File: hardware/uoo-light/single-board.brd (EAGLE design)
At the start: 49.5 x 48.3 mm, 27 parts

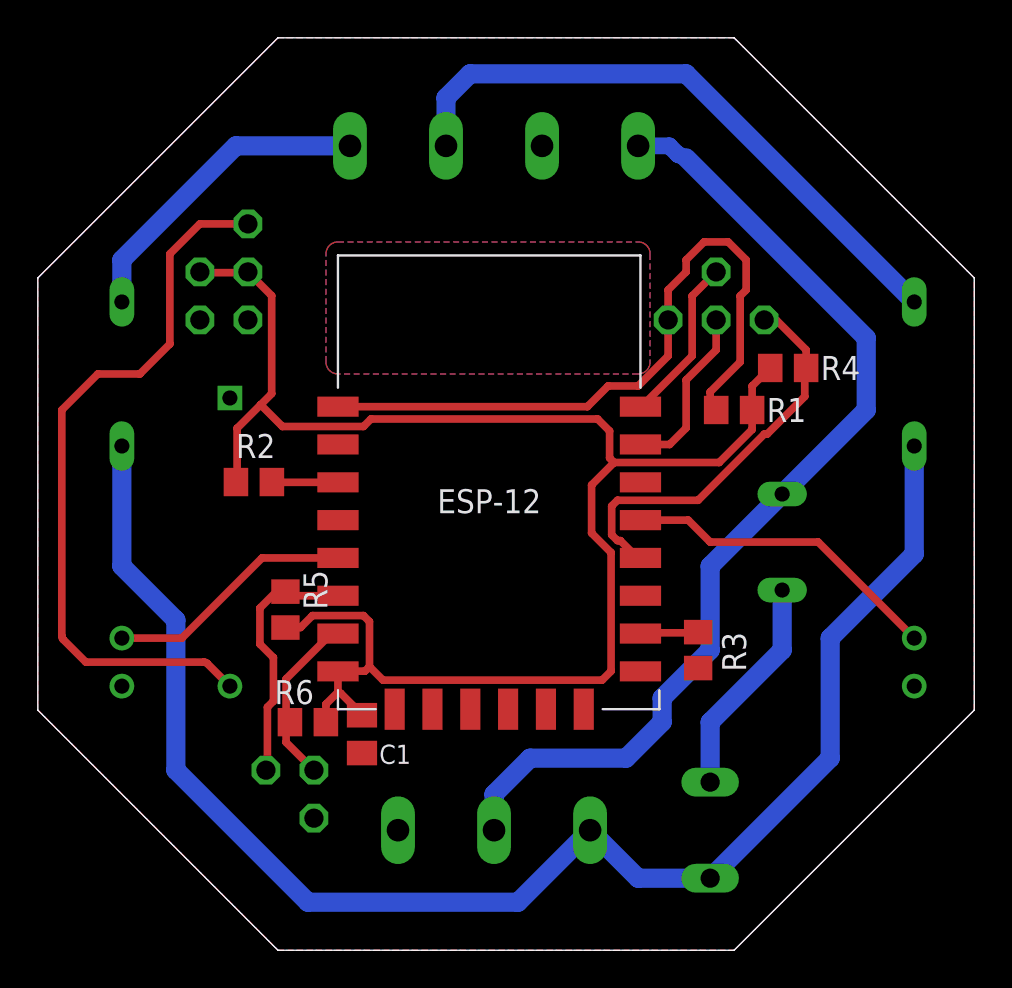
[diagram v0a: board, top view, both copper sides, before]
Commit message: second version of board. Mirrored elecromagnetic reeds, shorter pads in esp-12, better paths.added mount hole, bigger holes in my elements in library.
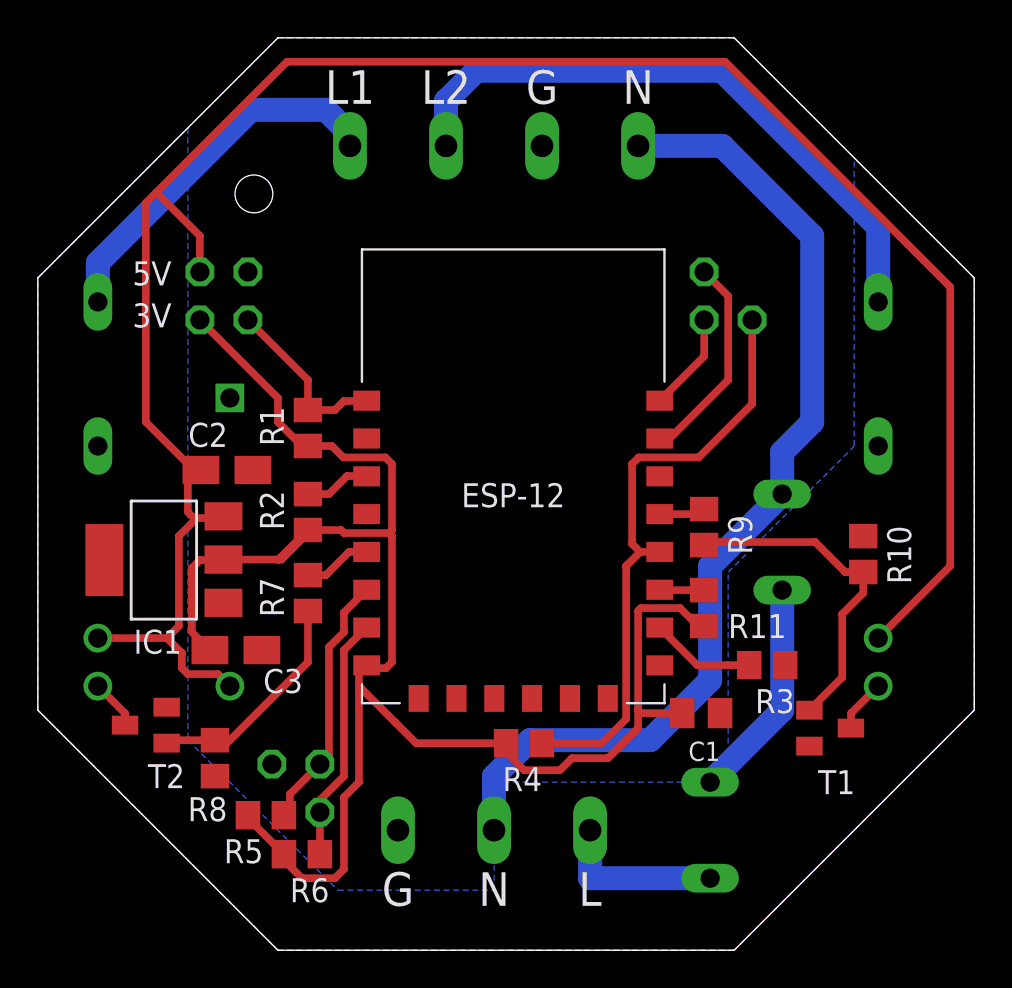
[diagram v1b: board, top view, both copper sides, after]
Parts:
- removed 3V1: 3V, pinhead:1X01
- removed GND8: GND, pinhead:1X01
- added C2, C3: (no value), rcl:A/3216-18R
- added IC1: REG1117, burr-brown:SOT223
- added R10, R11, R7, R8, R9: (no value), rcl:R0805
- added T1, T2: BC847, transistor:SOT23
- C1: value (none) -> 100nF
- G: value (none) -> G
- IN: value (none) -> AC IN
- L: value (none) -> LOUT
- OUT: value (none) -> OUT
- S1: value (none) -> S1
- S2: value (none) -> S2
- moved R4 24.3 mm to (28.9, 14.1)
- moved R1 22.6 mm to (17.5, 30.8), turned to 90 degrees
- moved RST 22.2 mm to (14.3, 36.5)
- moved C1 18.0 mm to (38.3, 15.7), turned to 180 degrees
- moved R5 10.9 mm to (15.2, 10.3), turned to 0 degrees
- moved R6 6.99 mm to (17.1, 8.26), turned to 0 degrees
- moved AC/DC 5.71 mm to (27.9, 24.8)
- moved R3 3.74 mm to (41.8, 18.3), turned to 0 degrees
- moved G 3.62 mm to (15.6, 13.0)
- moved 5V 3.59 mm to (11.7, 39.1)
- moved GND 3.59 mm to (14.3, 39.1)
- moved R2 3.27 mm to (17.5, 26.4), turned to 90 degrees
- moved S1 2.88 mm to (18.1, 13.0)
- moved RX 2.62 mm to (38.4, 39.1)
- moved TX 2.62 mm to (38.4, 36.5)
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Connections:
- new net N$12: T2.3, U$2.-
- new net N$13: T1.3, U$3.-
- new net N$14: R7.2, R8.1, T2.1
- new net N$16: R10.1, R9.2, T1.1
- new net N$17: ESP-12.P$17, R11.1
- net +3V3: now also C3.+, IC1.2, R11.2; no longer 3V1.1
- net GND: now also C2.-, C3.-, IC1.1, R10.2, R8.2, T1.2, T2.2; no longer GND8.1, U$2.-, U$3.-
- net REL1: now also R7.1; no longer U$2.+
- net REL2: now also R9.1; no longer U$3.+
- net VCC: now also C2.+, IC1.3, U$2.+, U$3.+
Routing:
- net VCC: track 38.7 -> 111.5 mm
- net L: track 79.4 -> 8.89 mm
- net N$1: track 37.1 -> 9.39 mm
- net N$16: track 0.00 -> 17.7 mm
- net REL2: track 17.1 -> 2.57 mm
- net N$14: track 0.00 -> 12.4 mm
- net N$4: track 21.5 -> 32.1 mm
- net REL1: track 13.2 -> 3.62 mm
- net +3V3: track 87.3 -> 93.5 mm
- net N$5: track 9.01 -> 5.26 mm
- net SW2: track 9.55 -> 13.0 mm
- net N$9: track 16.8 -> 19.9 mm
- net N$13: track 0.00 -> 2.82 mm
- net N$12: track 0.00 -> 2.66 mm
- net N$3: track 3.20 -> 5.55 mm
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- added copper zone on layer 16, net L
- removed copper zone on layer 16, net N$10
- removed copper zone on layer 1, net N$11
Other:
- board text added: ".pl"
- board text added: "G"
- board text added: "L"
- board text added: "L1"
- board text added: "L2"
- board text added: "N"
- board text added: "uoo-light"
